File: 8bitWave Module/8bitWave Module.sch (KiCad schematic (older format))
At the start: 44 parts, among them IC1 0.96_I2C_OLED, IC2 0.91_I2C_OLED, J1 REM, J2 EAR, J3 EXTENSION, M1 Mounting, M2 Mounting, M3 Mounting, M4 Mounting, SW1 UP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

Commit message: PAM8403
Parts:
- removed IC2: 0.91_I2C_OLED, i2c_oled:0.91_I2C_OLED, symbol I2C_OLED:0.91_I2C_OLED
- removed JP2: NO_FILTER, Pin_Headers:Pin_Header_Straight_1x02_Pitch2.54mm, symbol Device:Jumper_NO_Small
- removed JP3: AMPLIFY, Pin_Headers:Pin_Header_Straight_1x03_Pitch2.54mm, symbol Device:Jumper_NC_Dual
- removed RV1: 10k, Potentiometers:Potentiometer_Triwood_RM-065, symbol 8bitWave-Module-rescue:POT
- added A3: GF1002, gf1002:GF1002_reverse, symbol gf1002:GF1002
- added D3: 1n4001, Diodes_THT:D_DO-41_SOD81_P10.16mm_Horizontal, symbol barrel_jack:reverse_protect
- added J4: DC IN, Connectors:BARREL_JACK, symbol barrel_jack:barrel_9v
- added J5: LP_FILTER, Pin_Headers:Pin_Header_Straight_2x03_Pitch2.54mm, symbol conn:Conn_02x03_Odd_Even
- added J6: SPI, Pin_Headers:Pin_Header_Straight_1x03_Pitch2.54mm, symbol conn:Conn_01x03
- added J7: EAR_SEL, Pin_Headers:Pin_Header_Straight_2x06_Pitch2.54mm, symbol conn:Conn_02x06_Odd_Even
- added JP6: PWR_SEL, Pin_Headers:Pin_Header_Straight_1x03_Pitch2.54mm, symbol Jumper:Jumper_3_Bridged12
- added RV2: 10k, pot_vertical:Potentiometer_Trimmer_Bourns_3296W, symbol 8bitWave-Module-rescue:POT
- C10: value 100uF -> 220uF
- C9: value 10pF -> 47nF
- JP1: footprint Pin_Headers:Pin_Header_Straight_1x02_Pitch2.54mm -> Pin_Headers:Pin_Header_Straight_1x03_Pitch2.54mm; symbol Device:Jumper_NO_Small -> Jumper:Jumper_3_Bridged12
- R5: value 100 -> 10
- R6, R7: value 220 -> 330
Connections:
- net labels added: AUD_LINE, GF1002+, GF1002-, LM386+, VIN, V_EXT
- wire segments 158 -> 204
- no-connect marks 12 -> 15
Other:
- note added: "(Mainly used with MSX-line of computers)"
- note added: "01-02 Direct\n11-12"
- note added: "03-04 Direct (AC)\n11-12"
- note added: "05-06 LM386*\n11-12"
- note added: "07-08 GF1002\n09-10"
- note added: "1-2 Disabled*"
- note added: "3-4 Enabled\n5-6"
- note added: "AMPLIFIER OPTION #1 (GF1002)"
- note added: "AMPLIFIER OPTION #2 (LM386)"
- note added: "AUDIO OUTPUT SELECT"
- note added: "Based on the DigiWavuino, but I wanted to build my own version of it with a lot of\nfeatures no one would ever need - mostly because I wanted to play around with\nvarious things Arduino. There is an option for using either an 128x32 or 128x64 OLED,\ninstall whichever you want and hope that the software supports it - preferably, use one\nof the available faceplates and install the display there in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"
- note added: "LOW-PASS FILTER"
- note added: "Noise-reduction"
- note added: "PWR_SEL positions 1-2 is used when powering amplifier from\nvia Arduino, or when connecting a 5v supply directly. Positions\n2-3 is used when powering the entire circuit using a 9-12v DC \nsupply. Unjumpered, the amplifier and the rest of the circuit will\neach need their own power source."
- note removed: "Based on the DigiWavuino, but I wanted to build my own version of it with a lot of\nfeatures no one would ever need - mostly because I wanted to play around with\nvarious things Arduino. There is an option for using either an 128x32 or 128x64 OLED,\ninstall whichever you want and hope that the software supports it - alternatively, use\none of the available faceplates and install the display there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"
- note removed: "Noise\n-reduction"
- moved on the sheet: A1, A2, C1, C10, C2, C3, C4, C5, C6, C7, C8, C9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

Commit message: Gerber export
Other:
- note added: "Based on the DigiWavuino, but I wanted to build my own version of it with a lot of\nfeatures no one would ever need - mostly because I wanted to play around with\nvarious things Arduino. A 128x64 OLED can be used directly, but the main goal of\nthe project was to hide most things behind a faceplate instead,"
- note removed: "Based on the DigiWavuino, but I wanted to build my own version of it with a lot of\nfeatures no one would ever need - mostly because I wanted to play around with\nvarious things Arduino. There is an option for using either an 128x32 or 128x64 OLED,\ninstall whichever you want and hope that the software supports it - preferably, use one\nof the available faceplates and install the display there in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"
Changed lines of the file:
@@
 OLEDs usually work\nin either position,\nlink pins 1-2 for 3.3v.
 Text Notes 11850 10475 0    60   ~ 0
-Based on the DigiWavuino, but I wanted to build my own version of it with a lot of\nfeatures no one would ever need - mostly because I wanted to play around with\nvarious things Arduino. There is an option for using either an 128x32 or 128x64 OLED,\ninstall whichever you want and hope that the software supports it - preferably, use one\nof the available faceplates and install the display there instead.
+Based on the DigiWavuino, but I wanted to build my own version of it with a lot of\nfeatures no one would ever need - mostly because I wanted to play around with\nvarious things Arduino. A 128x64 OLED can be used directly, but the main goal of\nthe project was to hide most things behind a faceplate instead,
 Wire Wire Line
 	13825 6050 13825 6125

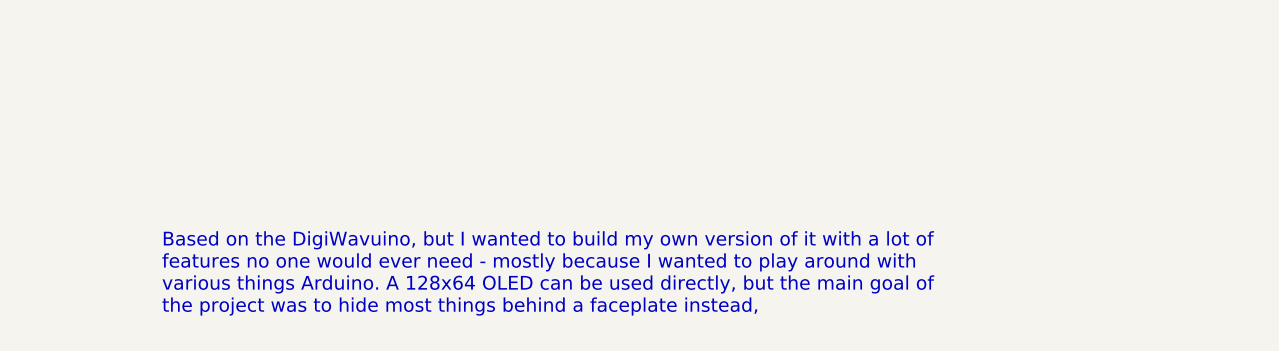
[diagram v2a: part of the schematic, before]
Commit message: Moved bypass cap, gain jumpers
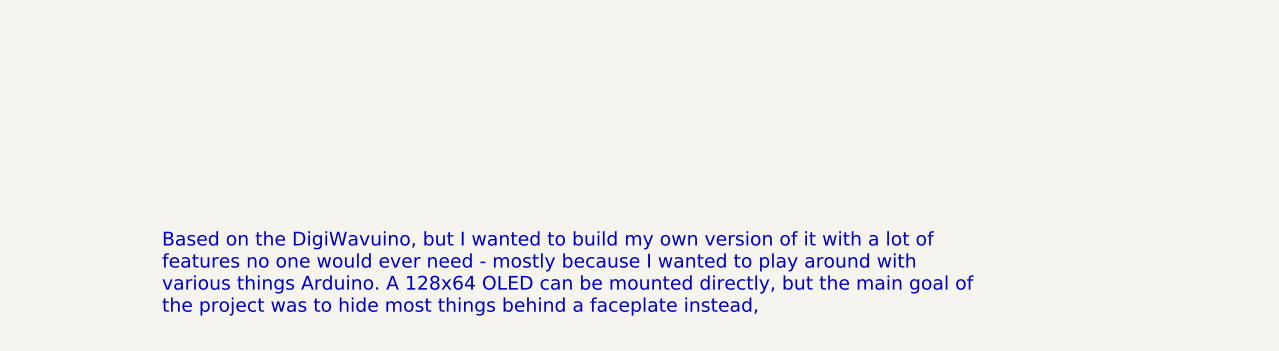
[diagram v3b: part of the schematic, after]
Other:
- note added: "Based on the DigiWavuino, but I wanted to build my own version of it with a lot of\nfeatures no one would ever need - mostly because I wanted to play around with\nvarious things Arduino. A 128x64 OLED can be mounted directly, but the main goal of\nthe project was to hide most things behind a faceplate instead,"
- note removed: "Based on the DigiWavuino, but I wanted to build my own version of it with a lot of\nfeatures no one would ever need - mostly because I wanted to play around with\nvarious things Arduino. A 128x64 OLED can be used directly, but the main goal of\nthe project was to hide most things behind a faceplate instead,"
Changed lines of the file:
@@
 OLEDs usually work\nin either position,\nlink pins 1-2 for 3.3v.
 Text Notes 11850 10475 0    60   ~ 0
-Based on the DigiWavuino, but I wanted to build my own version of it with a lot of\nfeatures no one would ever need - mostly because I wanted to play around with\nvarious things Arduino. A 128x64 OLED can be used directly, but the main goal of\nthe project was to hide most things behind a faceplate instead,
+Based on the DigiWavuino, but I wanted to build my own version of it with a lot of\nfeatures no one would ever need - mostly because I wanted to play around with\nvarious things Arduino. A 128x64 OLED can be mounted directly, but the main goal of\nthe project was to hide most things behind a faceplate instead,
 Wire Wire Line
 	13825 6050 13825 6125

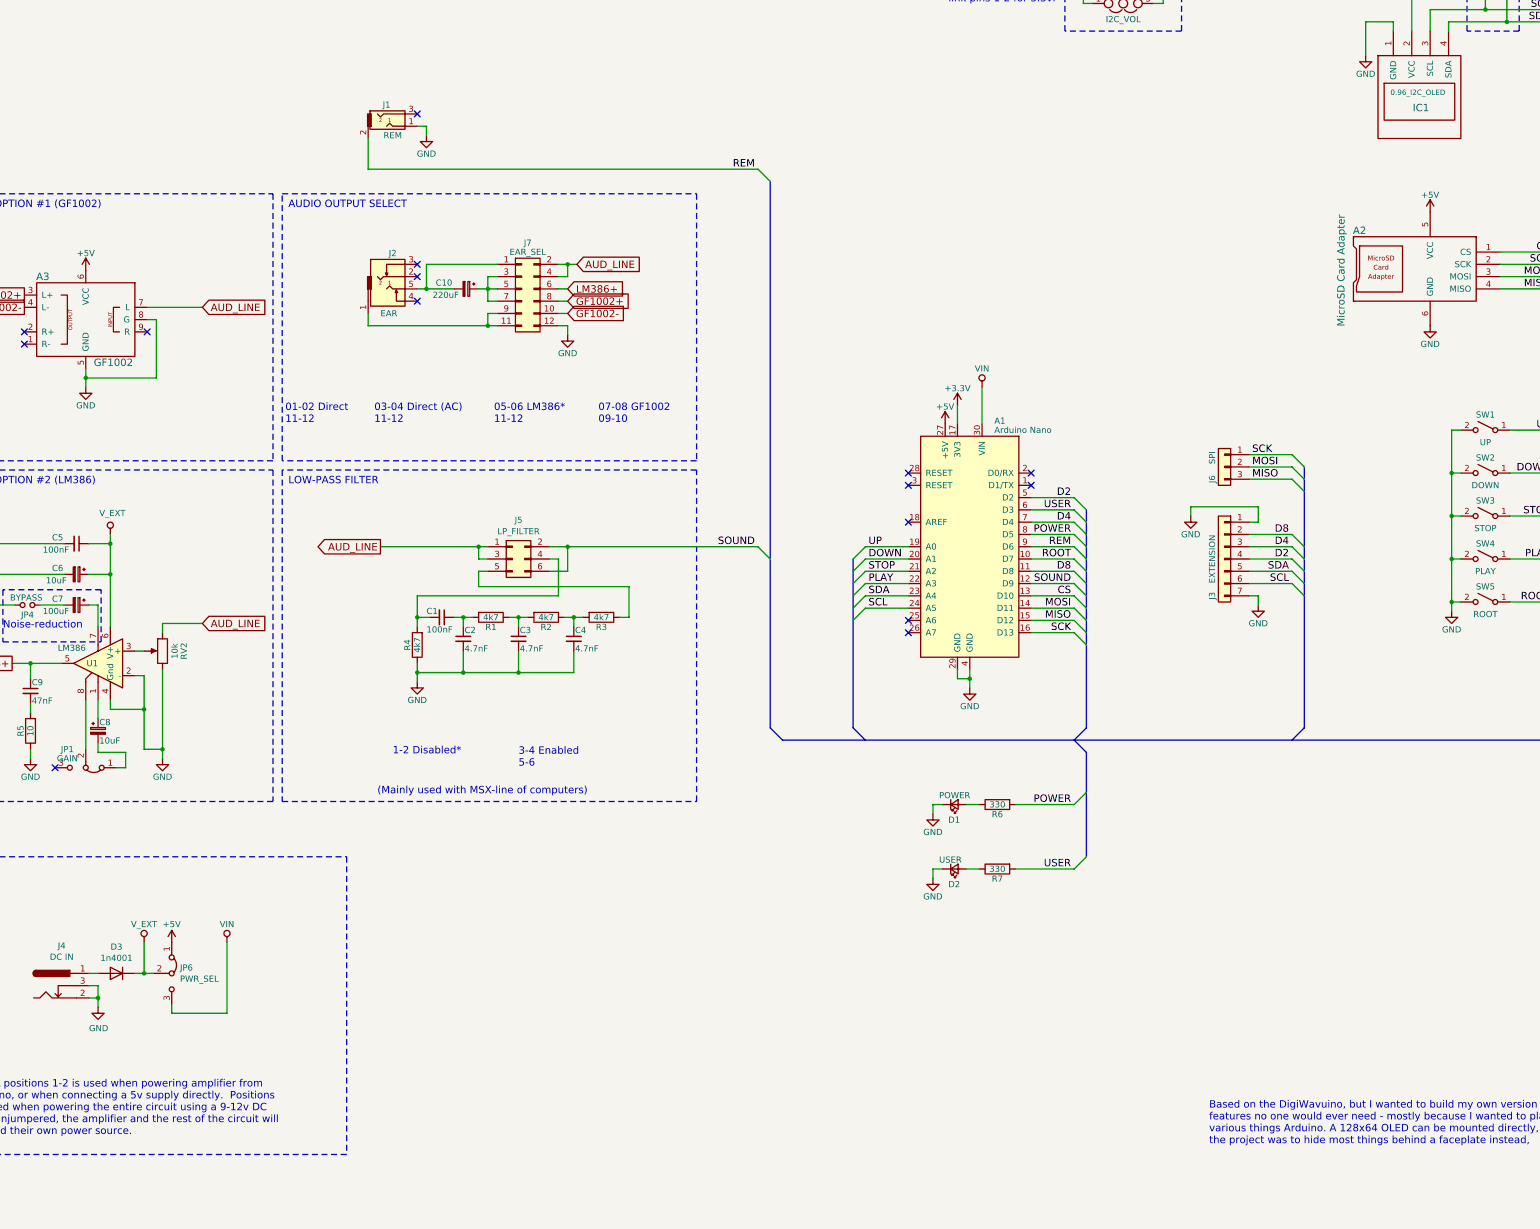
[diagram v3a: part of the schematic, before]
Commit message: Added bypass cap
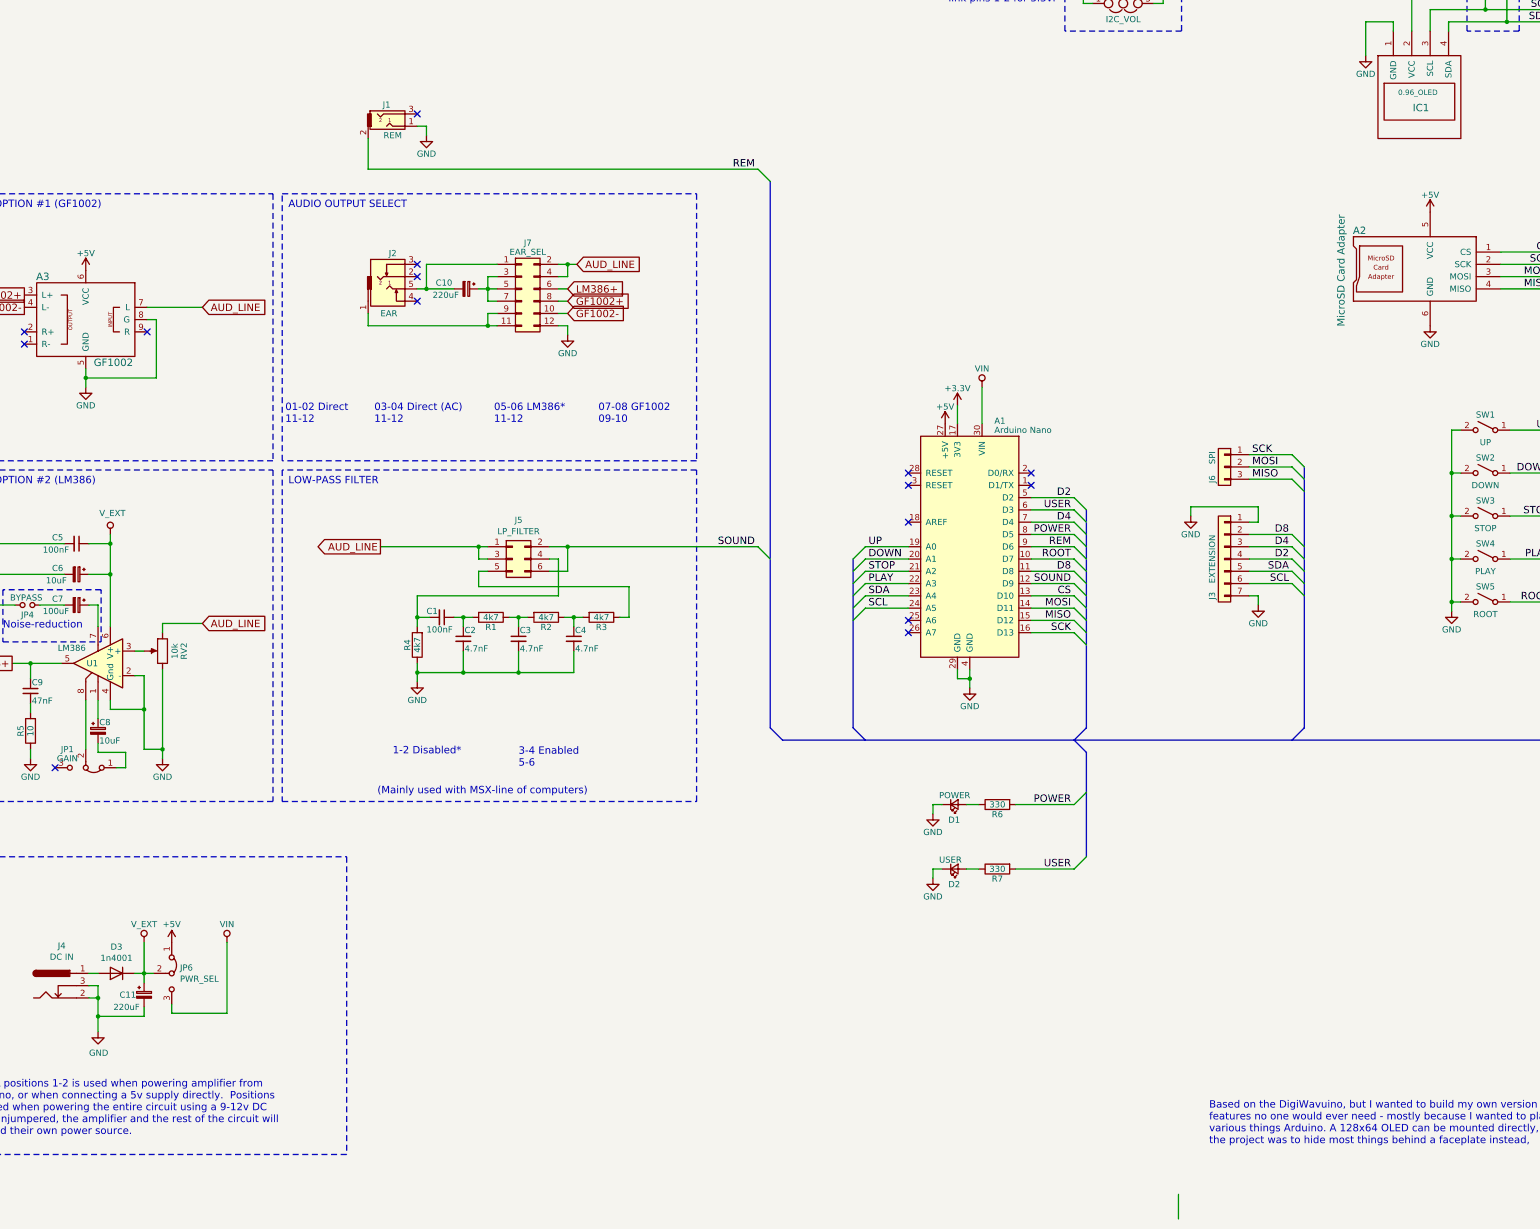
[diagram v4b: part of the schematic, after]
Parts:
- added C11: 220uF, Capacitors_THT:CP_Radial_D6.3mm_P2.50mm, symbol Device:CP_Small
- IC1: value 0.96_I2C_OLED -> 0.96_OLED
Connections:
- net GND: now also C11.2
- net VEXT: now also C11.1
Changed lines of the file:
@@
 P 13575 1850
 F 0 "IC1" H 13575 1675 60  0000 C CNN
-F 1 "0.96_I2C_OLED" H 13550 1800 43  0000 C CNN
+F 1 "0.96_OLED" H 13550 1800 43  0000 C CNN
 F 2 "i2c_oled:0.96_I2C_OLED" H 13575 2475 60  0001 C CNN
 F 3 "" H 13575 2475 60  0001 C CNN
@@
 L power:GND #PWR0101
 U 1 1 5E61DE6E
-P 2800 9350
-F 0 "#PWR0101" H 2800 9100 50  0001 C CNN
-F 1 "GND" H 2805 9177 50  0000 C CNN
-F 2 "" H 2800 9350 50  0001 C CNN
-F 3 "" H 2800 9350 50  0001 C CNN
-	1    2800 9350
-	1    0    0    -1
-$EndComp
-Wire Wire Line
-	2800 9350 2800 9275
+P 2800 9550
+F 0 "#PWR0101" H 2800 9300 50  0001 C CNN
+F 1 "GND" H 2805 9377 50  0000 C CNN
+F 2 "" H 2800 9550 50  0001 C CNN
+F 3 "" H 2800 9550 50  0001 C CNN
+	1    2800 9550
+	1    0    0    -1
+$EndComp
 Wire Wire Line
 	2800 9275 2725 9275
@@
 Wire Wire Line
 	2800 7275 2800 7200
+$Comp
+L Device:CP_Small C11
+U 1 1 5EDF6CF1
+P 3175 9250
+F 0 "C11" H 2975 9250 50  0000 L CNN
+F 1 "220uF" H 2925 9150 50  0000 L CNN
+F 2 "Capacitors_THT:CP_Radial_D6.3mm_P2.50mm" H 3175 9250 50  0001 C CNN
+F 3 "" H 3175 9250 50  0001 C CNN
+	1    3175 9250
+	1    0    0    -1
+$EndComp
+Wire Wire Line
+	11600 11075 11600 10875
+Wire Wire Line
+	2800 9275 2800 9425
+Wire Wire Line
+	3175 9350 3175 9425
+Wire Wire Line
+	3175 9425 2800 9425
+Connection ~ 2800 9425
+Wire Wire Line
+	2800 9425 2800 9550
+Wire Wire Line
+	3175 9150 3175 9075
 Wire Bus Line
 	8275 2625 8275 7075

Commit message: Updated faceplate A1 (KiCad 5)
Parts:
- J3: symbol conn:Conn_01x07 -> 8bitWave-Module-rescue:Conn_01x07-conn-8bitWave-Module-rescue
- J5: symbol conn:Conn_02x03_Odd_Even -> 8bitWave-Module-rescue:Conn_02x03_Odd_Even-conn-8bitWave-Module-rescue
- J6: symbol conn:Conn_01x03 -> 8bitWave-Module-rescue:Conn_01x03-conn-8bitWave-Module-rescue
- J7: symbol conn:Conn_02x06_Odd_Even -> 8bitWave-Module-rescue:Conn_02x06_Odd_Even-conn-8bitWave-Module-rescue
- RV2: symbol 8bitWave-Module-rescue:POT -> 8bitWave-Module-rescue:POT-8bitWave-Module-rescue
- SW1, SW2, SW3, SW4, SW5: symbol switches:SW_SPST -> 8bitWave-Module-rescue:SW_SPST-switches-8bitWave-Module-rescue
- U1: symbol linear:LM386 -> 8bitWave-Module-rescue:LM386-linear-8bitWave-Module-rescue
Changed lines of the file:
@@
 $EndComp
 $Comp
-L switches:SW_SPST SW1
+L 8bitWave-Module-rescue:SW_SPST-switches-8bitWave-Module-rescue SW1
 U 1 1 5E3B6481
 P 14100 4650
@@
 $EndComp
 $Comp
-L switches:SW_SPST SW2
+L 8bitWave-Module-rescue:SW_SPST-switches-8bitWave-Module-rescue SW2
 U 1 1 5E3B64CB
 P 14100 5000
@@
 $EndComp
 $Comp
-L switches:SW_SPST SW3
+L 8bitWave-Module-rescue:SW_SPST-switches-8bitWave-Module-rescue SW3
 U 1 1 5E3B64F8
 P 14100 5350
@@
 $EndComp
 $Comp
-L switches:SW_SPST SW4
+L 8bitWave-Module-rescue:SW_SPST-switches-8bitWave-Module-rescue SW4
 U 1 1 5E3B6550
 P 14100 5700
@@
 $EndComp
 $Comp
-L switches:SW_SPST SW5
+L 8bitWave-Module-rescue:SW_SPST-switches-8bitWave-Module-rescue SW5
 U 1 1 5E3B65A5
 P 14100 6050
@@
 $EndComp
 $Comp
-L linear:LM386 U1
+L 8bitWave-Module-rescue:LM386-linear-8bitWave-Module-rescue U1
 U 1 1 5E3CBAD8
 P 2800 6550
@@
 POWER
 $Comp
-L conn:Conn_01x07 J3
+L 8bitWave-Module-rescue:Conn_01x07-conn-8bitWave-Module-rescue J3
 U 1 1 5E3D299E
 P 11975 5700
@@
 PWR_SEL positions 1-2 is used when powering amplifier from\nvia Arduino, or when connecting a 5v supply directly.  Positions\n2-3 is used when powering the entire circuit using a 9-12v DC \nsupply. Unjumpered, the amplifier and the rest of the circuit will\neach need their own power source.
 $Comp
-L conn:Conn_02x03_Odd_Even J5
+L 8bitWave-Module-rescue:Conn_02x03_Odd_Even-conn-8bitWave-Module-rescue J5
 U 1 1 5E7A4F51
 P 6175 5700
@@
 LOW-PASS FILTER
 $Comp
-L conn:Conn_01x03 J6
+L 8bitWave-Module-rescue:Conn_01x03-conn-8bitWave-Module-rescue J6
 U 1 1 5EC476AB
 P 11975 4950
@@
 AUD_LINE
 $Comp
-L conn:Conn_02x06_Odd_Even J7
+L 8bitWave-Module-rescue:Conn_02x06_Odd_Even-conn-8bitWave-Module-rescue J7
 U 1 1 5F81D312
 P 6250 3500
@@
 	13500 775  13500 1400
 $Comp
-L 8bitWave-Module-rescue:POT RV2
+L 8bitWave-Module-rescue:POT-8bitWave-Module-rescue RV2
 U 1 1 5FF950C5
 P 3325 6450
